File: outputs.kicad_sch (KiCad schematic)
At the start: 46 parts, among them Q1 SQ2362CES, Q3 SQ2362CES, Q6 SQ2362CES, Q7 SQ2362CES, Q8 SQ2362CES, U2 LM393, U5 LM393

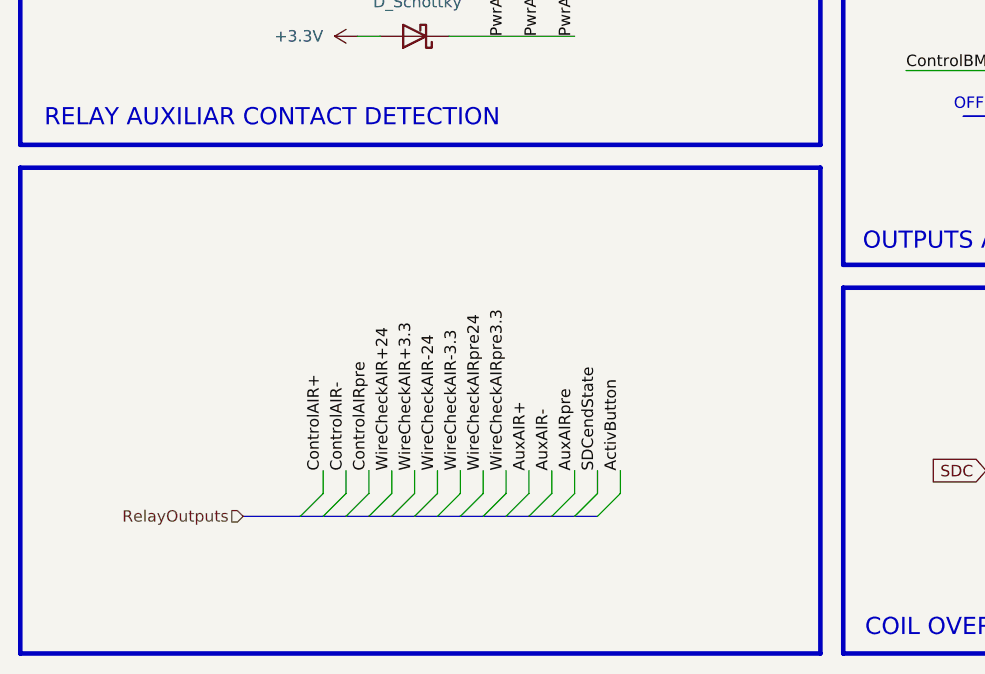
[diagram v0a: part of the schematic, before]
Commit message: correció dels outputs al GPIO
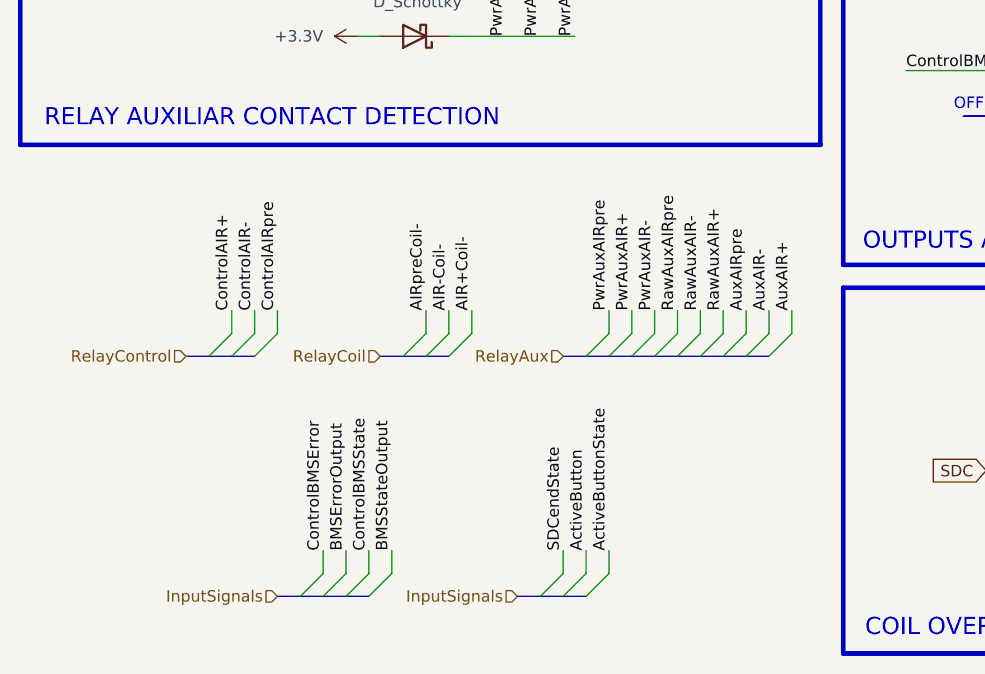
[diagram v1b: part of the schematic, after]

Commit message: Canvi de microcontrolador Control dels relés de potència actualitzat Leds afegits per a visualitzar l'estat del fusible
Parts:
- removed U5: LM393, Package_SO:TSSOP-8_4.4x3mm_P0.65mm, symbol Comparator:LM393
- added unit 3 of U2
- added unit 2 of U2
- C12, C13, C14, C15, C27: footprint Capacitor_SMD:C_0603_1608Metric -> Capacitor_SMD:C_0603_1608Metric_Pad1.08x0.95mm_HandSolder
- F2, F5, F6: footprint (none) -> Fuse:Fuse_1206_3216Metric_Pad1.42x1.75mm_HandSolder
- R1, R5, R7: footprint Resistor_SMD:R_1206_3216Metric -> Resistor_SMD:R_0201_0603Metric_Pad0.64x0.40mm_HandSolderResistor_SMD:R_0201_0603Metric_Pad0.64x0.40mm_HandSolder
- R15, R16, R2, R24, R3, R4, R6, R8, R9: footprint Resistor_SMD:R_1206_3216Metric -> Resistor_SMD:R_0201_0603Metric_Pad0.64x0.40mm_HandSolder
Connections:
- net +5V: now also U2.6 (-)
- net GND: now also U2.4 (V-)
- net SDC: no longer D8.2 (A)
- net SDCendState: now also U2.7
- net at C27.1, R15.1, R16.1: now also U2.5 (+)
- new net +24V: U2.8 (V+)
- new net SDCinput: D8.2 (A)

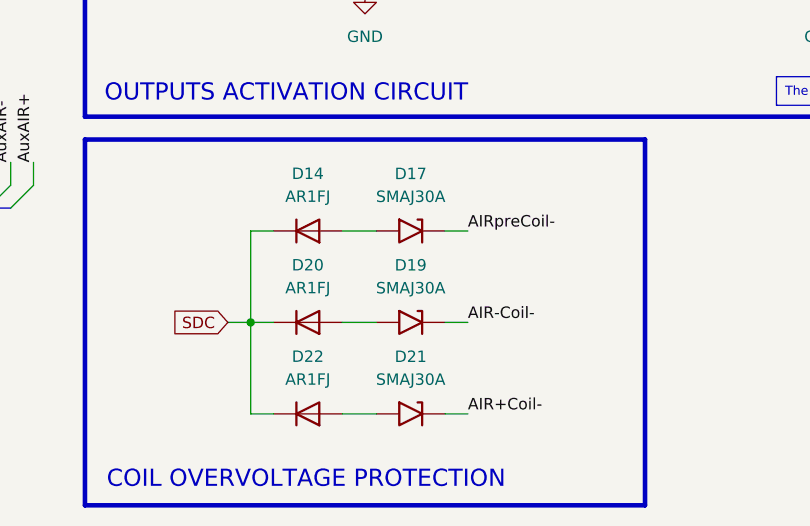
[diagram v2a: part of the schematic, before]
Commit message: - Outputs i inputs del ADBMS6822 acabats de configurar i assignar - TVS eliminat del circuit de descàrrega dels AIRs
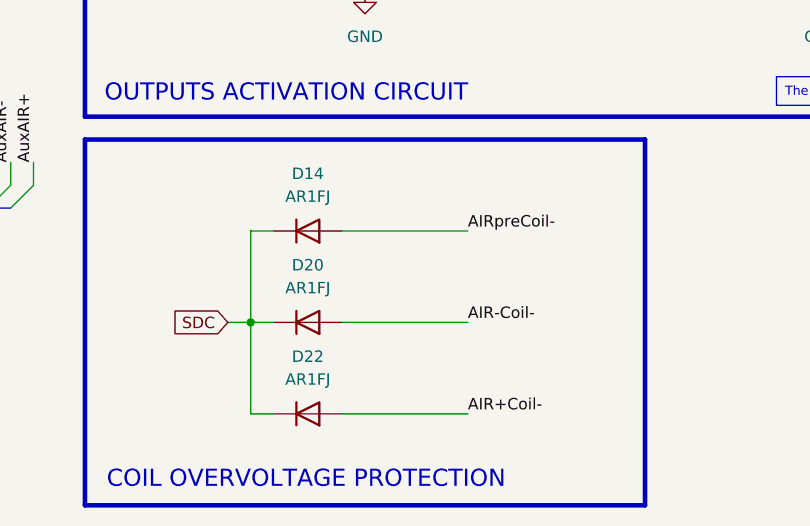
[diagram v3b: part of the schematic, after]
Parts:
- removed D17, D19, D21: SMAJ30A, Diode_SMD:D_SMA, symbol Diode:SMAJ30A
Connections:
- net AIR+Coil-: now also D22.2 (A)
- net AIR-Coil-: now also D20.2 (A)
- net AIRpreCoil-: now also D14.2 (A)
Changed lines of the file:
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@@
 	(wire
 		(pts
-			(xy 144.78 185.42) (xy 140.97 185.42)
+			(xy 140.97 185.42) (xy 154.94 185.42)
 		)
 		(stroke
@@
 	(wire
 		(pts
-			(xy 154.94 175.26) (xy 152.4 175.26)
-		)
-		(stroke
-			(width 0)
-			(type default)
-		)
-	)
-	(wire
-		(pts
 			(xy 128.27 175.26) (xy 130.81 175.26)
 		)
@@
 	(wire
 		(pts
-			(xy 154.94 185.42) (xy 152.4 185.42)
-		)
-		(stroke
-			(width 0)
-			(type default)
-		)
-	)
-	(wire
-		(pts
 			(xy 246.38 100.33) (xy 243.84 100.33)
 		)
@@
 	(wire
 		(pts
-			(xy 154.94 165.1) (xy 152.4 165.1)
-		)
-		(stroke
-			(width 0)
-			(type default)
-		)
-	)
-	(wire
-		(pts
 			(xy 49.53 71.12) (xy 49.53 73.66)
 		)
@@
 	(wire
 		(pts
-			(xy 144.78 175.26) (xy 140.97 175.26)
+			(xy 140.97 175.26) (xy 154.94 175.26)
 		)
 		(stroke
@@
 	(wire
 		(pts
-			(xy 144.78 165.1) (xy 140.97 165.1)
+			(xy 140.97 165.1) (xy 154.94 165.1)
 		)
 		(stroke
@@
 	)
 	(symbol
-		(lib_id "Diode:SMAJ30A")
-		(at 148.59 165.1 0)
-		(mirror y)
-		(unit 1)
-		(exclude_from_sim no)
-		(in_bom yes)
-		(on_board yes)
-		(dnp no)
-		(fields_autoplaced yes)
-		(property "Reference" "D17"
-			(at 148.59 158.75 0)
-			(effects
-				(font
-					(size 1.27 1.27)
-				)
-			)
-		)
-		(property "Value" "SMAJ30A"
-			(at 148.59 161.29 0)
-			(effects
-				(font
-					(size 1.27 1.27)
-				)
-			)
-		)
-		(property "Footprint" "Diode_SMD:D_SMA"
-			(at 148.59 170.18 0)
-			(effects
-				(font
-					(size 1.27 1.27)
-				)
-				(hide yes)
-			)
-		)
-		(property "Datasheet" "https://www.littelfuse.com/media?resourcetype=datasheets&itemid=75e32973-b177-4ee3-a0ff-cedaf1abdb93&filename=smaj-datasheet"
-			(at 149.86 165.1 0)
-			(effects
-				(font
-					(size 1.27 1.27)
-				)
-				(hide yes)
-			)
-		)
-		(property "Description" "400W unidirectional Transient Voltage Suppressor, 30.0Vr, SMA(DO-214AC)"
-			(at 148.59 165.1 0)
-			(effects
-				(font
-					(size 1.27 1.27)
-				)
-				(hide yes)
-			)
-		)
-		(pin "1"
-		)
-		(pin "2"
-		)
-		(instances
-			(project "BMSems"
-				(path "/241310d7-2595-46fd-a468-4bac14ba2b52/0534aeae-6f70-40f7-b035-12d510ac20ae"
-					(reference "D17")
-					(unit 1)
-				)
-			)
-		)
-	)
-	(symbol
 		(lib_id "power:GND")
 		(at 243.84 29.21 270)
@@
 	)
 	(symbol
-		(lib_id "Diode:SMAJ30A")
-		(at 148.59 175.26 0)
-		(mirror y)
-		(unit 1)
-		(exclude_from_sim no)
-		(in_bom yes)
-		(on_board yes)
-		(dnp no)
-		(fields_autoplaced yes)
-		(property "Reference" "D19"
-			(at 148.59 168.91 0)
-			(effects
-				(font
-					(size 1.27 1.27)
-				)
-			)
-		)
-		(property "Value" "SMAJ30A"
-			(at 148.59 171.45 0)
-			(effects
-				(font
-					(size 1.27 1.27)
-				)
-			)
-		)
-		(property "Footprint" "Diode_SMD:D_SMA"
-			(at 148.59 180.34 0)
-			(effects
-				(font
-					(size 1.27 1.27)
-				)
-				(hide yes)
-			)
-		)
-		(property "Datasheet" "https://www.littelfuse.com/media?resourcetype=datasheets&itemid=75e32973-b177-4ee3-a0ff-cedaf1abdb93&filename=smaj-datasheet"
-			(at 149.86 175.26 0)
-			(effects
-				(font
-					(size 1.27 1.27)
-				)
-				(hide yes)
-			)
-		)
-		(property "Description" "400W unidirectional Transient Voltage Suppressor, 30.0Vr, SMA(DO-214AC)"
-			(at 148.59 175.26 0)
-			(effects
-				(font
-					(size 1.27 1.27)
-				)
-				(hide yes)
-			)
-		)
-		(pin "1"
-		)
-		(pin "2"
-		)
-		(instances
-			(project "BMSems"
-				(path "/241310d7-2595-46fd-a468-4bac14ba2b52/0534aeae-6f70-40f7-b035-12d510ac20ae"
-					(reference "D19")
-					(unit 1)
-				)
-			)
-		)
-	)
-	(symbol
 		(lib_id "power:+3.3V")
 		(at 58.42 127 90)
@@
 					(unit 1)
 				)
-			)
-		)
-	)
-	(symbol
-		(lib_id "Diode:SMAJ30A")
-		(at 148.59 185.42 0)
-		(mirror y)
-		(unit 1)
-		(exclude_from_sim no)
-		(in_bom yes)
-		(on_board yes)
-		(dnp no)
-		(fields_autoplaced yes)
-		(property "Reference" "D21"
-			(at 148.59 179.07 0)
-			(effects
-				(font
-					(size 1.27 1.27)
-				)
-			)
-		)
-		(property "Value" "SMAJ30A"
-			(at 148.59 181.61 0)
-			(effects
-				(font
-					(size 1.27 1.27)
-				)
-			)
-		)
-		(property "Footprint" "Diode_SMD:D_SMA"
-			(at 148.59 190.5 0)
-			(effects
-				(font
-					(size 1.27 1.27)
-				)
-				(hide yes)
-			)
-		)
-		(property "Datasheet" "https://www.littelfuse.com/media?resourcetype=datasheets&itemid=75e32973-b177-4ee3-a0ff-cedaf1abdb93&filename=smaj-datasheet"
-			(at 149.86 185.42 0)
-			(effects
-				(font
-					(size 1.27 1.27)
-				)
-				(hide yes)
-			)
-		)
-		(property "Description" "400W unidirectional Transient Voltage Suppressor, 30.0Vr, SMA(DO-214AC)"
-			(at 148.59 185.42 0)
-			(effects
-				(font
-					(size 1.27 1.27)
-				)
-				(hide yes)
-			)
-		)
-		(pin "1"
-		)
-		(pin "2"
-		)
-		(instances
-			(project "BMSems"
-				(path "/241310d7-2595-46fd-a468-4bac14ba2b52/0534aeae-6f70-40f7-b035-12d510ac20ae"
-					(reference "D21")
-					(unit 1)
-				)

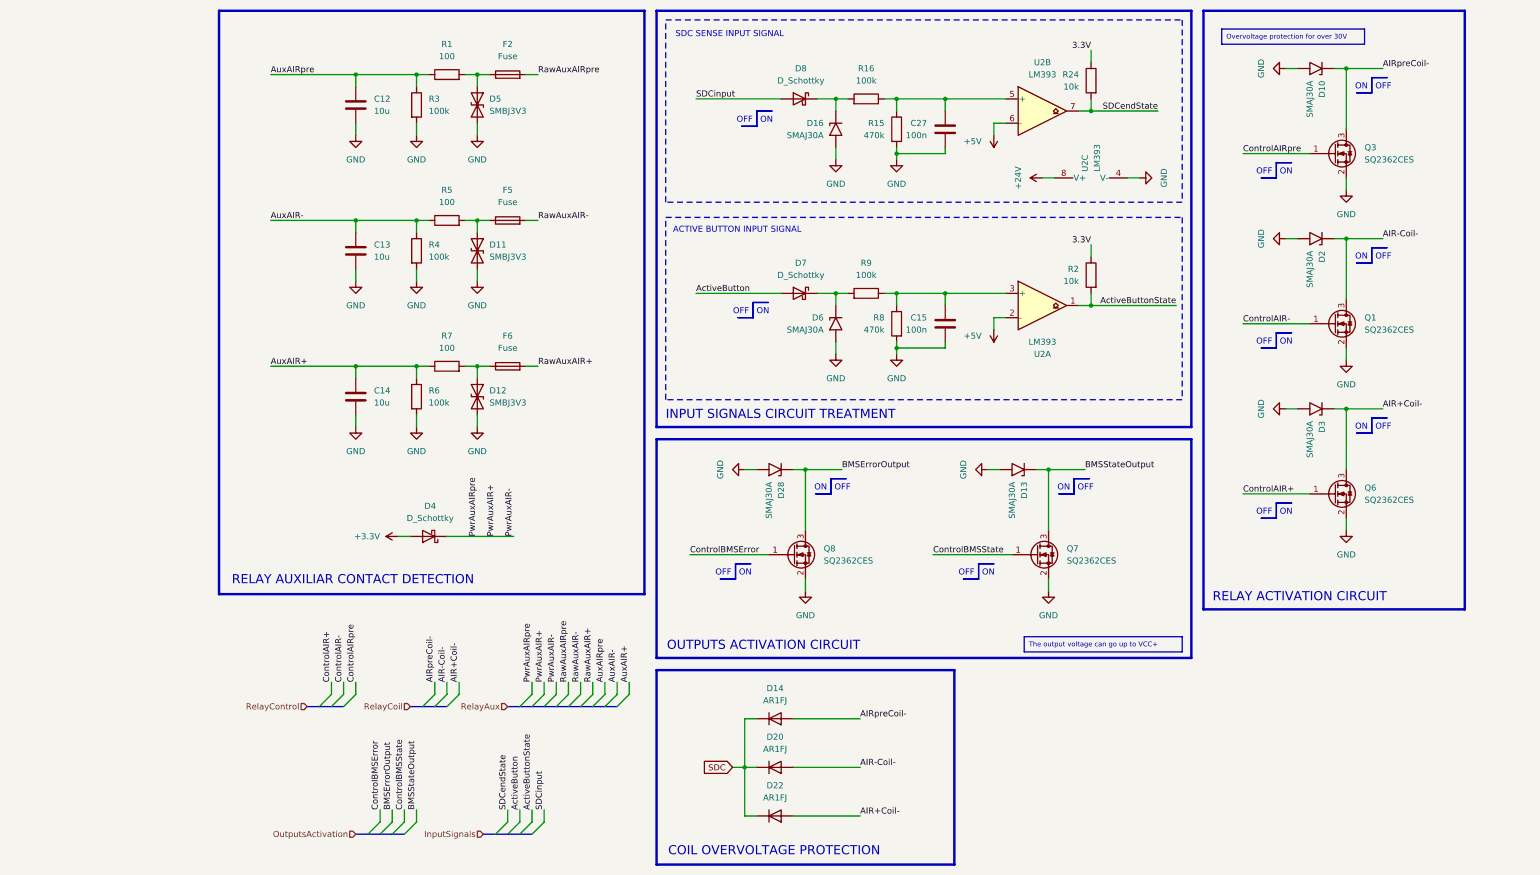
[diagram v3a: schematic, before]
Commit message: - Reorganització dels components al fitxer de stm32 - S'ha afegit el ADC ADS1113IDGS per la lectura del sensor Hall - Modificació del tranceptor CAN al SN65HVD234 - Eliminació del pin SWO - S'ha afegit el pin de enable per a cada tranceptor
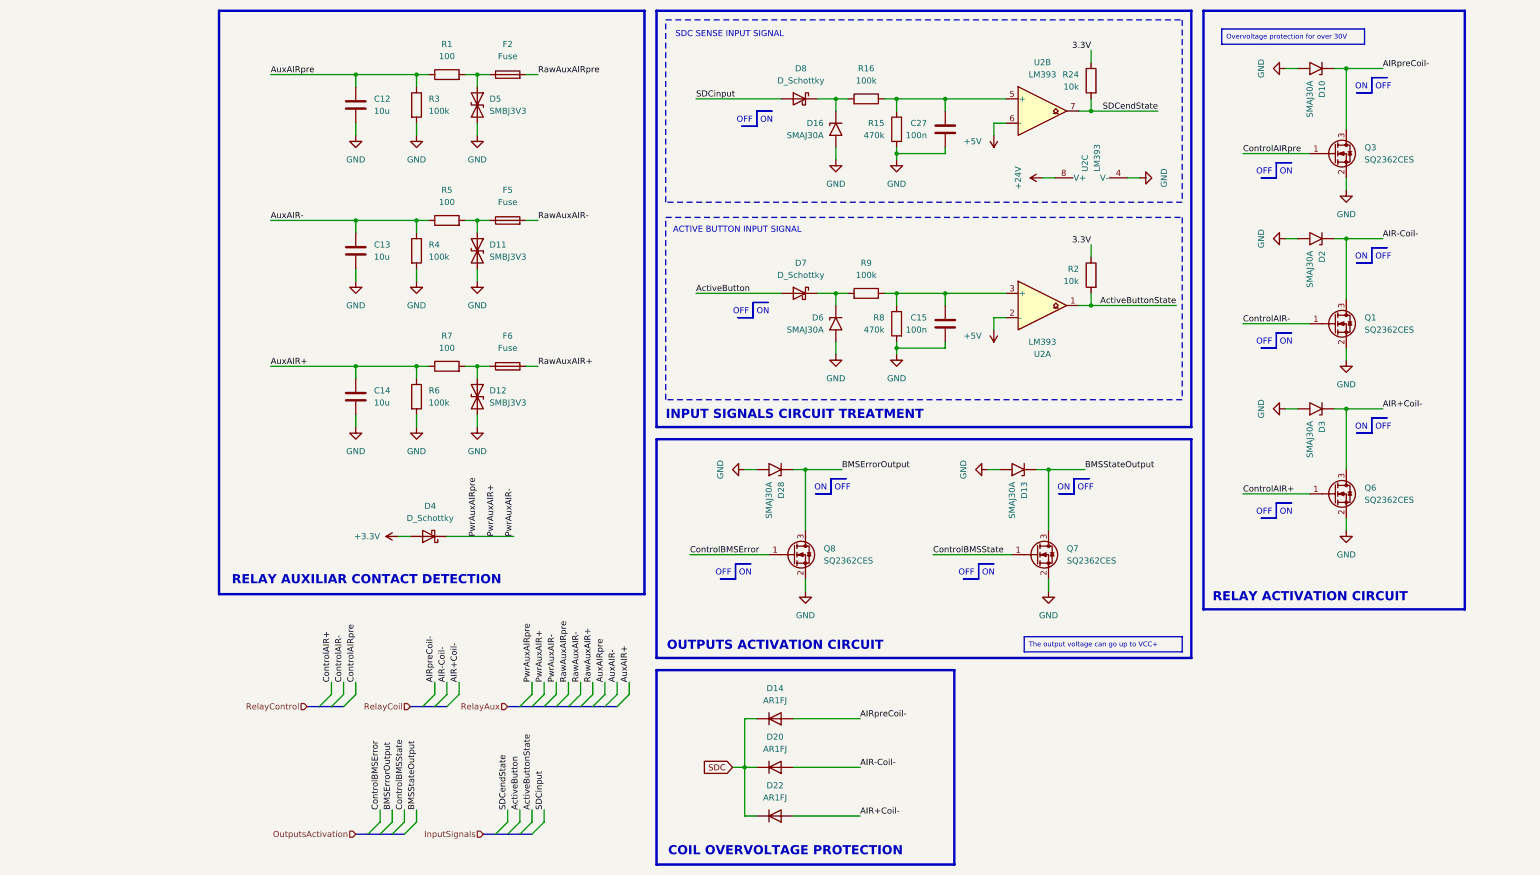
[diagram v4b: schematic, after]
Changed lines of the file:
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@@
 			(font
 				(size 1.905 1.905)
-				(thickness 0.2381)
+				(thickness 0.381)
+				(bold yes)
 			)
 			(justify left)
@@
 			(font
 				(size 1.905 1.905)
-				(thickness 0.2381)
+				(thickness 0.381)
+				(bold yes)
 			)
 			(justify left)
@@
 			(font
 				(size 1.905 1.905)
-				(thickness 0.2381)
+				(thickness 0.381)
+				(bold yes)
 			)
 			(justify left)
@@
 			(font
 				(size 1.905 1.905)
-				(thickness 0.2381)
+				(thickness 0.381)
+				(bold yes)
 			)
 			(justify left)
@@
 			(font
 				(size 1.905 1.905)
-				(thickness 0.2381)
+				(thickness 0.381)
+				(bold yes)
 			)
 			(justify left)

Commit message: S'ha afegit llista to do amb els canvis a fer i s'ha girat el circuit de l'entrada d'auxiliars per millor comprensió
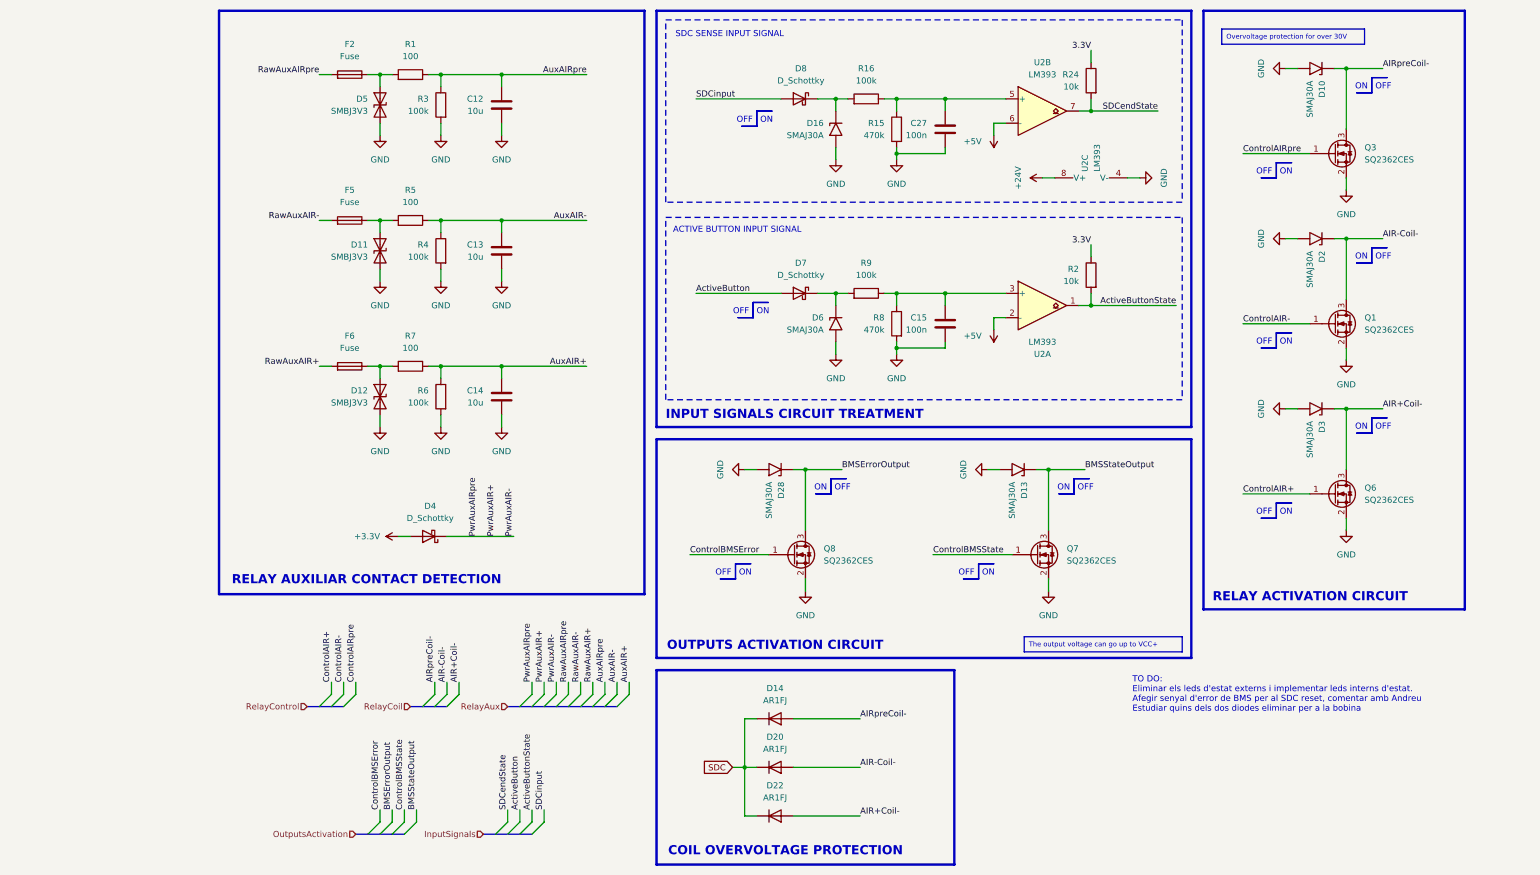
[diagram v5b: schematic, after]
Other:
- note added: "TO DO: Eliminar els leds d'estat externs i implementar leds interns d'estat. Afegir senyal d'error de BMS per al SDC reset, comentar amb Andreu Estudiar quins dels dos diodes eliminar per a la bobina"
- moved on the sheet: C12, C13, C14, D11, D12, D5, F2, F5, F6, R1, R3, R4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
